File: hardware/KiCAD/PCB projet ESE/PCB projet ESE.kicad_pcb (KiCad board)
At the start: 4 copper layers, 57 x 54 mm, 104 parts, among them J1 Conn_01x06, J10 Conn_01x06, J11 Conn_01x06, J12 Conn_01x06, J13 Conn_01x06, J14 Conn_01x06, J15 Conn_01x06, J16 Conn_01x03, J17 Conn_01x03, J18 Conn_01x03, J19 Conn_01x03, J2 Conn_01x04, J20 Conn_01x03, J21 Conn_01x03, J22 Conn_01x03, J23 Conn_01x03, J24 Conn_01x03, J25 Conn_01x03, J26 USB_C_Receptacle_USB2.0_16P, J3 Conn_01x06, J4 Conn_01x06, J5 Conn_01x04, J6 Conn_01x02, J7 Conn_ST_STDC14, J8 Conn_01x06, J9 Conn_01x06, SW1 SW_SPST, SW2 472121010111, U1 ZXBM5210-SP, U2 ZXBM5210-SP, U3 STM32G474RETx, U4 ADXL343, U5 USBLC6-2SC6

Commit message: maj schematic et pinout
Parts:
- moved U3 0.59 mm to (249.0, 52.2)
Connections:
- net ADC renamed ADC1_IN2
- C13 pad 1: Net-(U3-VDDA) -> +3.3V
- C14 pad 2: Net-(U3-VDDA) -> +3.3V
- L1 pad 2: Net-(U3-VDDA) -> +3.3V
- U3 pad 29: Net-(U3-VDDA) -> +3.3V
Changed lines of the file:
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@@
 	(net 3 "+5V")
 	(net 4 "NRST")
-	(net 5 "ADC")
+	(net 5 "ADC1_IN2")
 	(net 6 "VBUS")
 	(net 7 "SDA TOF")
@@
 	(net 82 "unconnected-(SW2-Pad3)")
 	(net 83 "+7.4V")
-	(net 84 "Net-(U3-VDDA)")
-	(net 85 "Net-(C24-Pad1)")
-	(net 86 "Net-(C25-Pad1)")
-	(net 87 "PWM_Encodeur_B_Phase_1")
-	(net 88 "PWM_Encodeur_A_Phase_1")
-	(net 89 "unconnected-(J3-Pin_1-Pad1)")
-	(net 90 "unconnected-(J3-Pin_6-Pad6)")
-	(net 91 "PWM_Encodeur_B_Phase_2")
-	(net 92 "PWM_Encodeur_A_Phase_2")
-	(net 93 "Net-(J6-Pin_2)")
-	(net 94 "unconnected-(J26-SBU1-PadA8)")
-	(net 95 "Net-(J26-CC1)")
-	(net 96 "Net-(J26-CC2)")
-	(net 97 "unconnected-(J26-SBU2-PadB8)")
-	(net 98 "Net-(MP1-EN{slash}SYNC)")
-	(net 99 "PG_51")
-	(net 100 "Net-(MP2-EN{slash}SYNC)")
-	(net 101 "PG_52")
+	(net 84 "Net-(C24-Pad1)")
+	(net 85 "Net-(C25-Pad1)")
+	(net 86 "PWM_Encodeur_B_Phase_1")
+	(net 87 "PWM_Encodeur_A_Phase_1")
+	(net 88 "unconnected-(J3-Pin_1-Pad1)")
+	(net 89 "unconnected-(J3-Pin_6-Pad6)")
+	(net 90 "PWM_Encodeur_B_Phase_2")
+	(net 91 "PWM_Encodeur_A_Phase_2")
+	(net 92 "Net-(J6-Pin_2)")
+	(net 93 "unconnected-(J26-SBU1-PadA8)")
+	(net 94 "Net-(J26-CC1)")
+	(net 95 "Net-(J26-CC2)")
+	(net 96 "unconnected-(J26-SBU2-PadB8)")
+	(net 97 "Net-(MP1-EN{slash}SYNC)")
+	(net 98 "PG_51")
+	(net 99 "Net-(MP2-EN{slash}SYNC)")
+	(net 100 "PG_52")
 	(footprint "Connector_JST:JST_PH_B6B-PH-K_1x06_P2.00mm_Vertical"
 		(layer "F.Cu")
@@
 			(layers "F.Cu" "F.Mask" "F.Paste")
 			(roundrect_rratio 0.25)
-			(net 96 "Net-(J26-CC2)")
+			(net 95 "Net-(J26-CC2)")
 			(pintype "passive")
 		)
@@
 			(layers "*.Cu" "*.Mask")
 			(remove_unused_layers no)
-			(net 93 "Net-(J6-Pin_2)")
+			(net 92 "Net-(J6-Pin_2)")
 			(pinfunction "2")
 			(pintype "passive")
@@
 			(layers "F.Cu" "F.Mask" "F.Paste")
 			(roundrect_rratio 0.25)
-			(net 85 "Net-(C24-Pad1)")
+			(net 84 "Net-(C24-Pad1)")
 			(pintype "passive")
 		)
@@
 			(size 0.3 1.45)
 			(layers "F.Cu" "F.Mask" "F.Paste")
-			(net 95 "Net-(J26-CC1)")
+			(net 94 "Net-(J26-CC1)")
 			(pinfunction "CC1")
 			(pintype "bidirectional")
@@
 			(size 0.3 1.45)
 			(layers "F.Cu" "F.Mask" "F.Paste")
-			(net 94 "unconnected-(J26-SBU1-PadA8)")
+			(net 93 "unconnected-(J26-SBU1-PadA8)")
 			(pinfunction "SBU1")
 			(pintype "bidirectional+no_connect")
@@
 			(size 0.3 1.45)
 			(layers "F.Cu" "F.Mask" "F.Paste")
-			(net 96 "Net-(J26-CC2)")
+			(net 95 "Net-(J26-CC2)")
 			(pinfunction "CC2")
 			(pintype "bidirectional")
@@
 			(size 0.3 1.45)
 			(layers "F.Cu" "F.Mask" "F.Paste")
-			(net 97 "unconnected-(J26-SBU2-PadB8)")
+			(net 96 "unconnected-(J26-SBU2-PadB8)")
 			(pinfunction "SBU2")
 			(pintype "bidirectional+no_connect")
@@
 			(layers "*.Cu" "*.Mask")
 			(remove_unused_layers no)
-			(net 93 "Net-(J6-Pin_2)")
+			(net 92 "Net-(J6-Pin_2)")
 			(pinfunction "Pin_2")
 			(pintype "passive")
@@
 			(remove_unused_layers no)
 			(roundrect_rratio 0.208333)
-			(net 89 "unconnected-(J3-Pin_1-Pad1)")
+			(net 88 "unconnected-(J3-Pin_1-Pad1)")
 			(pinfunction "Pin_1")
 			(pintype "passive+no_connect")
@@
 			(layers "*.Cu" "*.Mask")
 			(remove_unused_layers no)
-			(net 90 "unconnected-(J3-Pin_6-Pad6)")
+			(net 89 "unconnected-(J3-Pin_6-Pad6)")
 			(pinfunction "Pin_6")
 			(pintype "passive+no_connect")
@@
 			(layers "F.Cu" "F.Mask" "F.Paste")
 			(roundrect_rratio 0.25)
-			(net 101 "PG_52")
+			(net 100 "PG_52")
 			(pintype "passive")
 		)
@@
 			(layers "*.Cu" "*.Mask")
 			(remove_unused_layers no)
-			(net 92 "PWM_Encodeur_A_Phase_2")
+			(net 91 "PWM_Encodeur_A_Phase_2")
 			(pinfunction "Pin_3")
 			(pintype "passive")
@@
 			(layers "*.Cu" "*.Mask")
 			(remove_unused_layers no)
-			(net 91 "PWM_Encodeur_B_Phase_2")
+			(net 90 "PWM_Encodeur_B_Phase_2")
 			(pinfunction "Pin_4")
 			(pintype "passive")
@@
 			(layers "F.Cu" "F.Mask" "F.Paste")
 			(roundrect_rratio 0.25)
-			(net 84 "Net-(U3-VDDA)")
+			(net 1 "+3.3V")
 			(pintype "passive")
 		)
@@
 			(layers "F.Cu" "F.Mask" "F.Paste")
 			(roundrect_rratio 0.15)
-			(net 101 "PG_52")
+			(net 100 "PG_52")
 			(pinfunction "PG")
 			(pintype "output")
@@
 			(layers "F.Cu" "F.Mask" "F.Paste")
 			(roundrect_rratio 0.15)
-			(net 100 "Net-(MP2-EN{slash}SYNC)")
+			(net 99 "Net-(MP2-EN{slash}SYNC)")
 			(pinfunction "EN/SYNC")
 			(pintype "input")
@@
 			(layers "F.Cu" "F.Mask" "F.Paste")
 			(roundrect_rratio 0.25)
-			(net 99 "PG_51")
+			(net 98 "PG_51")
 			(pintype "passive")
 		)
@@
 	(footprint "Package_QFP:LQFP-64_10x10mm_P0.5mm"
 		(layer "F.Cu")
-		(at 249.02 52.84)
+		(at 249 52.25)
 		(descr "LQFP, 64 Pin (https://www.analog.com/media/en/technical-documentation/data-sheets/ad7606_7606-6_7606-4.pdf), generated with kicad-footprint-generator ipc_gullwing_generator.py")
 		(tags "LQFP QFP")
@@
 			(layers "F.Cu" "F.Mask" "F.Paste")
 			(roundrect_rratio 0.25)
-			(net 99 "PG_51")
+			(net 98 "PG_51")
 			(pinfunction "PC13")
 			(pintype "bidirectional")
@@
 			(layers "F.Cu" "F.Mask" "F.Paste")
 			(roundrect_rratio 0.25)
-			(net 5 "ADC")
+			(net 5 "ADC1_IN2")
 			(pinfunction "PA1")
 			(pintype "bidirectional")
@@
 			(layers "F.Cu" "F.Mask" "F.Paste")
 			(roundrect_rratio 0.25)
-			(net 101 "PG_52")
+			(net 100 "PG_52")
 			(pinfunction "PC4")
 			(pintype "bidirectional")
@@
 			(layers "F.Cu" "F.Mask" "F.Paste")
 			(roundrect_rratio 0.25)
-			(net 88 "PWM_Encodeur_A_Phase_1")
+			(net 87 "PWM_Encodeur_A_Phase_1")
 			(pinfunction "PB0")
 			(pintype "bidirectional")
@@
 			(layers "F.Cu" "F.Mask" "F.Paste")
 			(roundrect_rratio 0.25)
-			(net 87 "PWM_Encodeur_B_Phase_1")
+			(net 86 "PWM_Encodeur_B_Phase_1")
 			(pinfunction "PB1")
 			(pintype "bidirectional")
@@
 			(layers "F.Cu" "F.Mask" "F.Paste")
 			(roundrect_rratio 0.25)
-			(net 84 "Net-(U3-VDDA)")
+			(net 1 "+3.3V")
 			(pinfunction "VDDA")
 			(pintype "power_in")
@@
 			(layers "F.Cu" "F.Mask" "F.Paste")
 			(roundrect_rratio 0.25)
-			(net 91 "PWM_Encodeur_B_Phase_2")
+			(net 90 "PWM_Encodeur_B_Phase_2")
 			(pinfunction "PB14")
 			(pintype "bidirectional")
@@
 			(layers "F.Cu" "F.Mask" "F.Paste")
 			(roundrect_rratio 0.25)
-			(net 92 "PWM_Encodeur_A_Phase_2")
+			(net 91 "PWM_Encodeur_A_Phase_2")
 			(pinfunction "PB6")
 			(pintype "bidirectional")
@@
 			(layers "F.Cu" "F.Mask" "F.Paste")
 			(roundrect_rratio 0.25)
-			(net 5 "ADC")
+			(net 5 "ADC1_IN2")
 			(pintype "passive")
 		)
@@
 			(layers "F.Cu" "F.Mask" "F.Paste")
 			(roundrect_rratio 0.25)
-			(net 5 "ADC")
+			(net 5 "ADC1_IN2")
 			(pintype "passive")
 		)
@@
 			(layers "F.Cu" "F.Mask" "F.Paste")
 			(roundrect_rratio 0.25)
-			(net 98 "Net-(MP1-EN{slash}SYNC)")
+			(net 97 "Net-(MP1-EN{slash}SYNC)")
 			(pintype "passive")
 		)
@@
 			(layers "F.Cu" "F.Mask" "F.Paste")
 			(roundrect_rratio 0.25)
-			(net 5 "ADC")
+			(net 5 "ADC1_IN2")
 			(pintype "passive")
 		)
@@
 			(layers "*.Cu" "*.Mask")
 			(remove_unused_layers no)
-			(net 88 "PWM_Encodeur_A_Phase_1")
+			(net 87 "PWM_Encodeur_A_Phase_1")
 			(pinfunction "Pin_3")
 			(pintype "passive")
@@
 			(layers "*.Cu" "*.Mask")
 			(remove_unused_layers no)
-			(net 87 "PWM_Encodeur_B_Phase_1")
+			(net 86 "PWM_Encodeur_B_Phase_1")
 			(pinfunction "Pin_4")
 			(pintype "passive")
@@
 			(layers "F.Cu" "F.Mask" "F.Paste")
 			(roundrect_rratio 0.25)
-			(net 100 "Net-(MP2-EN{slash}SYNC)")
+			(net 99 "Net-(MP2-EN{slash}SYNC)")
 			(pintype "passive")
 		)
@@
 			(layers "F.Cu" "F.Mask" "F.Paste")
 			(roundrect_rratio 0.25)
-			(net 86 "Net-(C25-Pad1)")
+			(net 85 "Net-(C25-Pad1)")
 			(pintype "passive")
 		)
@@
 			(layers "F.Cu" "F.Mask" "F.Paste")
 			(roundrect_rratio 0.25)
-			(net 84 "Net-(U3-VDDA)")
+			(net 1 "+3.3V")
 			(pintype "passive")
 		)
@@
 			(layers "F.Cu" "F.Mask" "F.Paste")
 			(roundrect_rratio 0.25)
-			(net 85 "Net-(C24-Pad1)")
+			(net 84 "Net-(C24-Pad1)")
 			(pintype "passive")
 		)
@@
 			(layers "F.Cu" "F.Mask" "F.Paste")
 			(roundrect_rratio 0.25)
-			(net 95 "Net-(J26-CC1)")
+			(net 94 "Net-(J26-CC1)")
 			(pintype "passive")
 		)
@@
 			(layers "F.Cu" "F.Mask" "F.Paste")
 			(roundrect_rratio 0.15)
-			(net 99 "PG_51")
+			(net 98 "PG_51")
 			(pinfunction "PG")
 			(pintype "output")
@@
 			(layers "F.Cu" "F.Mask" "F.Paste")
 			(roundrect_rratio 0.15)
-			(net 98 "Net-(MP1-EN{slash}SYNC)")
+			(net 97 "Net-(MP1-EN{slash}SYNC)")
 			(pinfunction "EN/SYNC")
 			(pintype "input")
@@
 			(layers "F.Cu" "F.Mask" "F.Paste")
 			(roundrect_rratio 0.25)
-			(net 84 "Net-(U3-VDDA)")
+			(net 1 "+3.3V")
 			(pintype "passive")
 		)
@@
 			(layers "F.Cu" "F.Mask" "F.Paste")
 			(roundrect_rratio 0.25)
-			(net 86 "Net-(C25-Pad1)")
+			(net 85 "Net-(C25-Pad1)")
 			(pintype "passive")
 		)

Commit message: update pcb
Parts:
- removed J17, J18, J19, J20, J21, J22, J23, J24, J25: Conn_01x03, Connector_JST:JST_PH_B3B-PH-K_1x03_P2.00mm_Vertical
- BUxxSD1, C1, C18, C19, C2, C20, C21, C22, C23, C24, C25, C26, C27, C28, C29, C3, C30, C31, C32, C33, C4, J1, J16, J4, J6, L2, L3, MP1, MP2, R10, R11, R12, R13, R14, R15, R16, R17, R18, R19, R20, R21, U1, U2: moved to B.Cu
- J10, J11, J12, J13, J14, J15, J3, J8, J9: footprint Connector_JST:JST_PH_B6B-PH-K_1x06_P2.00mm_Vertical -> Connector_JST:JST_SH_BM06B-SRSS-TB_1x06-1MP_P1.00mm_Vertical
- J2: footprint Connector_JST:JST_PH_B4B-PH-K_1x04_P2.00mm_Vertical -> Connector_JST:JST_SH_BM04B-SRSS-TB_1x04-1MP_P1.00mm_Vertical
- moved J7 180.2 mm to (84.3, 86.0)
- moved C4 175.5 mm to (87.8, 64.8), turned to -90 degrees
- moved U2 169.5 mm to (88.2, 70.0), turned to -90 degrees
- moved L1 167.8 mm to (95.2, 75.2), turned to 90 degrees
- moved C7 167.7 mm to (97.0, 75.2), turned to 90 degrees
- moved R3 167.1 mm to (96.3, 72.7), turned to -90 degrees
- moved R4 165.9 mm to (97.4, 72.7), turned to 90 degrees
- moved J4 165.1 mm to (83.0, 75.0), turned to 90 degrees
- moved J3 164.3 mm to (82.2, 59.5), turned to -90 degrees
- moved H2 164.1 mm to (84.0, 95.0)
- moved C14 157.6 mm to (108.0, 79.8)
- moved H1 155.3 mm to (84.0, 51.0)
- moved J5 154.0 mm to (93.0, 95.5)
- moved R2 150.1 mm to (113.5, 72.7), turned to 180 degrees
- moved R1 150.0 mm to (113.6, 71.6), turned to 180 degrees
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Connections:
- J1 pad 1: Encodeur phase A 1 -> Moteur - 1
- J1 pad 3: PWM_Encodeur_A_Phase_1 -> Encodeur_A_Phase_1
- J1 pad 4: PWM_Encodeur_B_Phase_1 -> Encodeur_B_Phase_1
- J1 pad 6: Encodeur Phase B 1 -> Moteur + 1
- J10 pad 1: INT -> INT_7
- J11 pad 1: INT -> INT_2
- J12 pad 1: INT -> INT_5
- J13 pad 1: INT -> INT_8
- J14 pad 1: INT -> INT_3
- J15 pad 1: INT -> INT_6
- J4 pad 1: Encodeur phase A 2 -> Moteur - 2
- J4 pad 3: PWM_Encodeur_A_Phase_2 -> Encodeur_A_Phase_2
- J4 pad 4: PWM_Encodeur_B_Phase_2 -> Encodeur_B_Phase_2
- J4 pad 6: Encodeur Phase B 2 -> Moteur + 2
- J8 pad 1: INT -> INT_1
- J9 pad 1: INT -> INT_4
- U1 pad 1: Encodeur phase A 1 -> Moteur + 1
- U1 pad 7: Encodeur Phase B 1 -> Moteur - 1
- U2 pad 1: Encodeur phase A 2 -> Moteur + 2
- U2 pad 7: Encodeur Phase B 2 -> Moteur - 2
- U3 pad 10: PWM_servo_3 -> unconnected-(U3-PC2-Pad10)
- U3 pad 11: PWM_servo_4 -> unconnected-(U3-PC3-Pad11)
- U3 pad 12: PWM_servo_5 -> INT_8
- U3 pad 21: STBY_IN -> XSHUT_8
- U3 pad 24: PWM_Encodeur_A_Phase_1 -> INT_4
- U3 pad 25: PWM_Encodeur_B_Phase_1 -> INT_3
- U3 pad 30: PWM_servo_7 -> INT_6
- U3 pad 33: PWM_servo_8 -> INT_5
- U3 pad 36: PWM_Encodeur_B_Phase_2 -> INT_7
- U3 pad 38: PWM FWD 2 -> Encodeur_A_Phase_2
- U3 pad 39: PWM REV 2 -> Encodeur_B_Phase_2
- U3 pad 56: PWM_servo_6 -> INT_2
- U3 pad 58: PWM_LED2 -> INT_1
- U3 pad 59: PWM_Encodeur_A_Phase_2 -> PWM FWD 2
- U3 pad 62: XSHUT_8 -> PWM REV 2
- U3 pad 8: PWM_servo_1 -> Encodeur_B_Phase_1
- U3 pad 9: PWM_servo_2 -> Encodeur_A_Phase_1
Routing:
- net +3.3V: track 0.00 -> 26.6 mm
- net +5V: track 0.00 -> 23.6 mm
- net +7.4V: track 0.00 -> 23.2 mm
- net VBUS: track 0.00 -> 12.8 mm
- net D+: track 0.00 -> 11.2 mm, vias 0 -> 2
- net GND: track 0.00 -> 10.6 mm
- net Net-(C25-Pad1): track 0.00 -> 5.98 mm
- net D-: track 0.00 -> 5.80 mm, vias 0 -> 2
- net Net-(MP1-BST): track 0.00 -> 5.24 mm, vias 0 -> 2
- net PG_52: track 0.00 -> 4.69 mm, vias 0 -> 2
- net Net-(MP1-VCC): track 0.00 -> 4.08 mm
- net Net-(MP1-EN/SYNC): track 0.00 -> 3.96 mm
- net Net-(MP2-VCC): track 0.00 -> 3.95 mm
- net ADC1_IN2: track 0.00 -> 3.84 mm
- net Net-(C26-Pad1): track 0.00 -> 3.73 mm
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
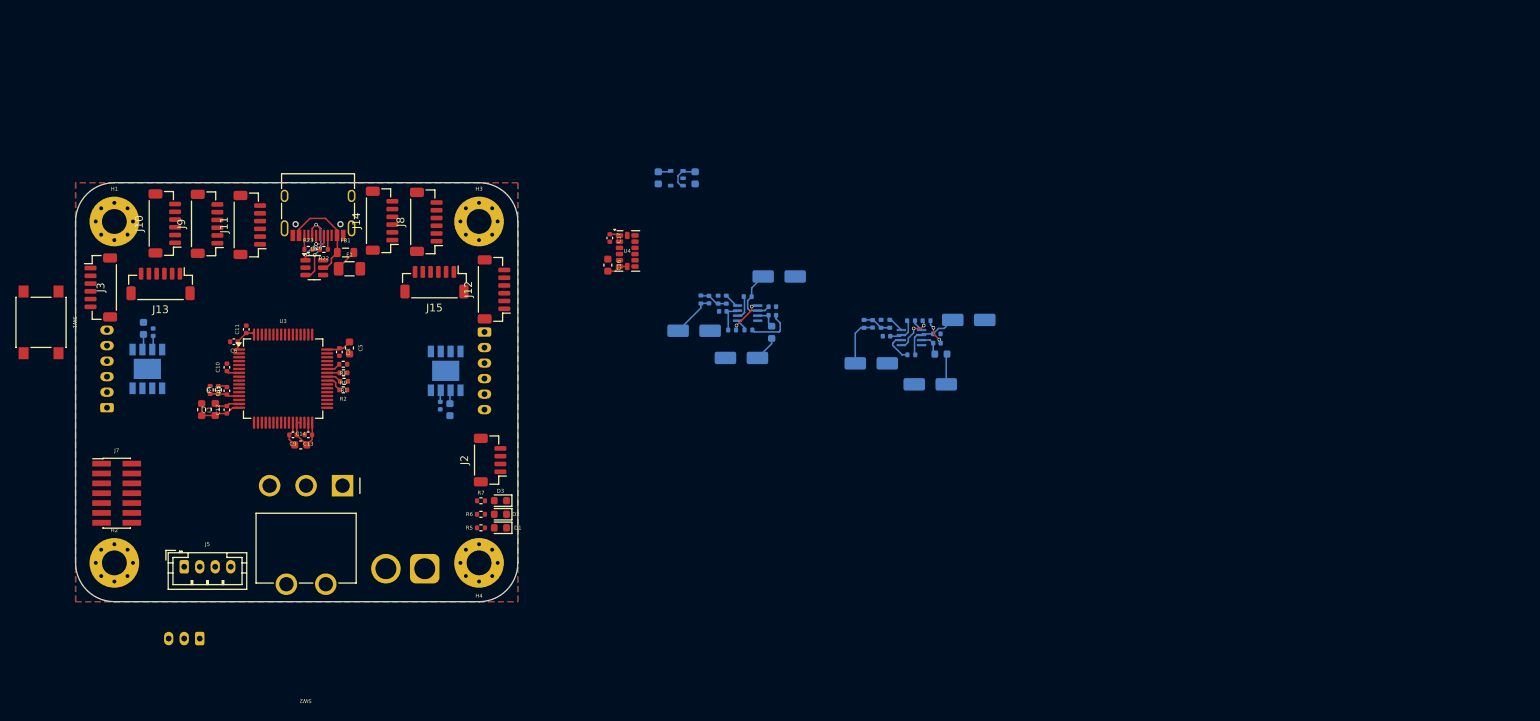
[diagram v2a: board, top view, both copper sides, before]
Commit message: modif pcb editor & sch for new uc pinout
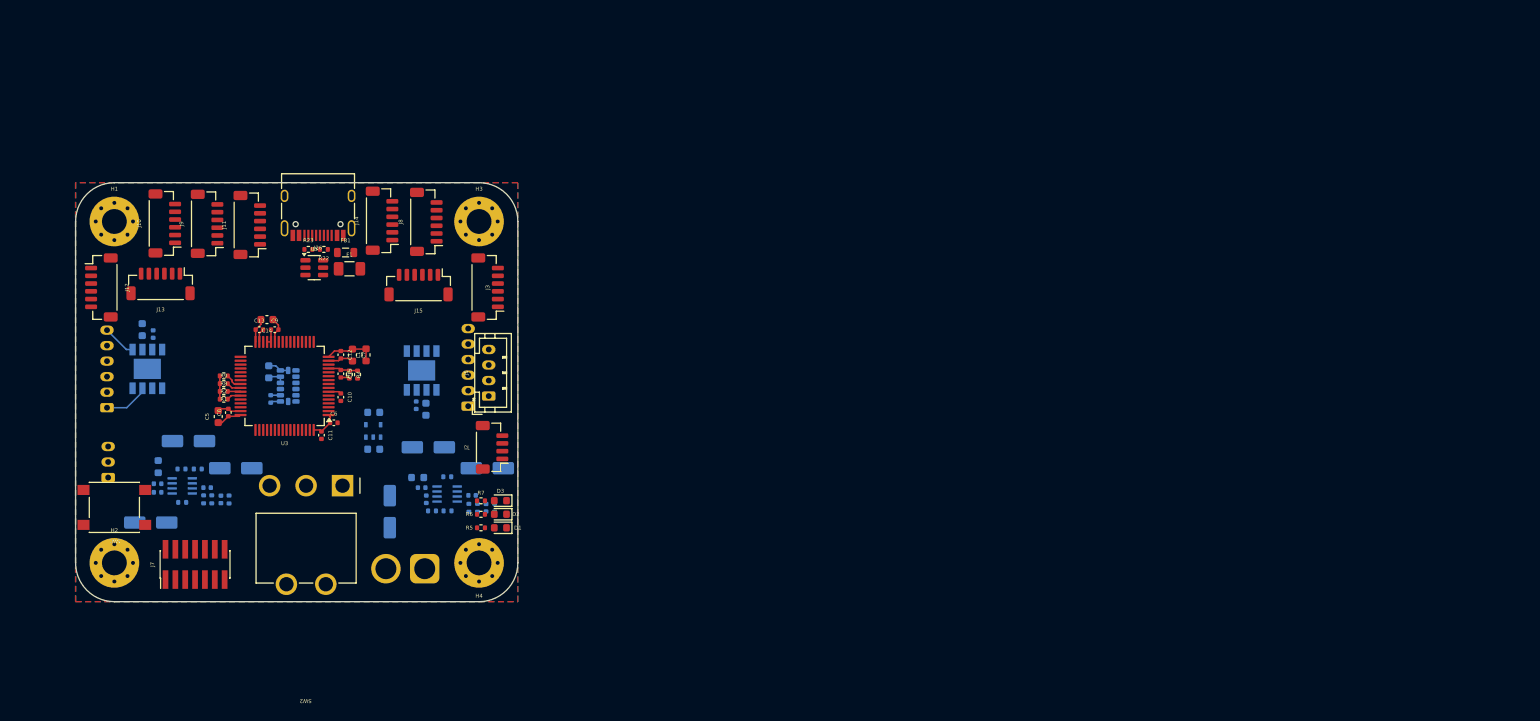
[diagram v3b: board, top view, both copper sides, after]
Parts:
- C16, C17, U4: moved to B.Cu
- moved C19 87.0 mm to (88.7, 89.8), turned to 0 degrees
- moved C23 82.8 mm to (89.6, 85.9), turned to 0 degrees
- moved C25 82.1 mm to (89.6, 84.8), turned to 0 degrees
- moved L3 80.9 mm to (89.7, 82.6), turned to 90 degrees
- moved C18 78.6 mm to (119.5, 88.4), turned to 90 degrees
- moved R11 77.6 mm to (92.7, 87.2), turned to 0 degrees
- moved MP2 76.2 mm to (92.8, 85.0), turned to 0 degrees
- moved R15 75.2 mm to (92.7, 82.9), turned to 180 degrees
- moved R17 72.1 mm to (95.5, 86.8), turned to -90 degrees
- moved C31 72.1 mm to (93.5, 79.3), turned to 180 degrees
- moved R13 71.2 mm to (94.8, 82.9), turned to 180 degrees
- moved C21 70.2 mm to (96.0, 85.3), turned to 0 degrees
- moved R19 70.2 mm to (96.5, 86.8), turned to -90 degrees
- moved L2 69.3 mm to (123.1, 84.0), turned to 180 degrees
- moved C22 69.2 mm to (124.2, 86.8), turned to 90 degrees
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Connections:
- J7 pad 11: GND -> unconnected-(J7-GNDDetect-Pad11)
- J7 pad 12: NRST -> unconnected-(J7-~{RST}-Pad12)
- J7 pad 13: UART_Debug_RX -> unconnected-(J7-VCP_RX-Pad13)
- J7 pad 14: UART_Debug_TX -> unconnected-(J7-VCP_TX-Pad14)
- J7 pad 4: SWDIO -> unconnected-(J7-JTMS/SWDIO-Pad4)
- J7 pad 6: SWCLK -> unconnected-(J7-JCLK/SWCLK-Pad6)
- U3 pad 11: unconnected-(U3-PC3-Pad11) -> INT 2
- U3 pad 12: INT_8 -> INT 1
- U3 pad 14: UART_Debug_TX -> UART_HC05_TX
- U3 pad 17: UART_Debug_RX -> UART_HC05_RX
- U3 pad 18: INT 1 -> INT_6
- U3 pad 19: INT 2 -> XSHUT_6
- U3 pad 20: Lidar Output  -> INT_1
- U3 pad 21: XSHUT_8 -> XSHUT_1
- U3 pad 22: PG_52 -> INT_3
- U3 pad 23: XSHUT_4 -> XSHUT_3
- U3 pad 24: INT_4 -> XSHUT_2
- U3 pad 25: INT_3 -> INT_2
- U3 pad 26: XSHUT_7 -> XSHUT_4
- U3 pad 3: unconnected-(U3-PC14-Pad3) -> Lidar Output 
- U3 pad 30: INT_6 -> INT_4
- U3 pad 33: INT_5 -> XSHUT_7
- U3 pad 34: XSHUT_5 -> INT_7
- U3 pad 35: XSHUT_6 -> INT_8
- U3 pad 36: INT_7 -> XSHUT_8
- U3 pad 37: XSHUT_3 -> INT_5
- U3 pad 38: Encodeur_A_Phase_2 -> Encodeur_B_Phase_2
- U3 pad 39: Encodeur_B_Phase_2 -> Encodeur_A_Phase_2
- U3 pad 40: Accel SCL -> SCL TOF
- U3 pad 41: Accel SDA -> SDA TOF
- U3 pad 42: SCL TOF -> Accel SCL
- U3 pad 43: SDA TOF -> Accel SDA
- U3 pad 44: XSHUT_1 -> XSHUT_5
- U3 pad 51: XSHUT_2 -> PG_52
- U3 pad 52: UART_HC05_TX -> UART_Debug_TX
- U3 pad 53: UART_HC05_RX -> UART_Debug_RX
- U3 pad 56: INT_2 -> unconnected-(U3-PB3-Pad56)
- U3 pad 58: INT_1 -> unconnected-(U3-PB5-Pad58)
- U3 pad 59: PWM FWD 2 -> PWM REV 2
- U3 pad 60: PWM REV 1 -> PWM FWD 2
- U3 pad 61: PWM FWD 1 -> PWM REV 1
- U3 pad 62: PWM REV 2 -> PWM FWD 1
- U3 pad 8: Encodeur_B_Phase_1 -> Encodeur_A_Phase_1
- U3 pad 9: Encodeur_A_Phase_1 -> Encodeur_B_Phase_1
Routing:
- net +5V: track 23.6 -> 0.00 mm
- net +7.4V: track 23.2 -> 0.00 mm
- net VBUS: track 12.8 -> 0.00 mm
- net D+: track 11.2 -> 0.00 mm, vias 2 -> 0
- net Net-(C25-Pad1): track 5.98 -> 0.00 mm
- net Moteur - 2: track 0.00 -> 5.89 mm
- net D-: track 5.80 -> 0.00 mm, vias 2 -> 0
- net GND: track 10.6 -> 16.3 mm
- net Net-(MP1-BST): track 5.24 -> 0.00 mm, vias 2 -> 0
- net PG_52: track 4.69 -> 0.00 mm, vias 2 -> 0
- net Moteur + 2: track 0.00 -> 4.33 mm
- net Net-(MP1-VCC): track 4.08 -> 0.00 mm
- net Net-(MP1-EN/SYNC): track 3.96 -> 0.00 mm
- net Net-(MP2-VCC): track 3.95 -> 0.00 mm
- net Net-(C26-Pad1): track 3.73 -> 0.00 mm
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- added copper zone on In2.Cu, net Net-(J6-Pin_2)

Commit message: maj
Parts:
- turned F1 to 180 degrees
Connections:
- J7 pad 11: unconnected-(J7-GNDDetect-Pad11) -> GND
- J7 pad 12: unconnected-(J7-~{RST}-Pad12) -> NRST
- J7 pad 13: unconnected-(J7-VCP_RX-Pad13) -> UART_Debug_RX
- J7 pad 14: unconnected-(J7-VCP_TX-Pad14) -> UART_Debug_TX
- J7 pad 4: unconnected-(J7-JTMS/SWDIO-Pad4) -> SWDIO
- J7 pad 6: unconnected-(J7-JCLK/SWCLK-Pad6) -> SWCLK
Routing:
- net SDA TOF: track 1.88 -> 37.6 mm, vias 0 -> 2
- net SCL TOF: track 2.20 -> 32.3 mm
- net NRST: track 1.67 -> 24.6 mm
- net Encodeur_B_Phase_1: track 0.00 -> 19.3 mm
- net Encodeur_A_Phase_1: track 0.00 -> 18.7 mm, vias 0 -> 1
- net Moteur - 1: track 0.00 -> 13.3 mm, vias 0 -> 1
- net Moteur + 1: track 0.00 -> 9.59 mm
- net D+: track 0.00 -> 9.33 mm, vias 0 -> 2
- net Accel SDA: track 1.84 -> 10.4 mm, vias 0 -> 1
- net Accel SCL: track 1.67 -> 9.21 mm, vias 0 -> 1
- net PG_52: track 0.00 -> 4.80 mm, vias 0 -> 2
- net Net-(MP1-BST): track 0.00 -> 4.75 mm, vias 0 -> 2
- net INT 1: track 0.00 -> 4.31 mm, vias 0 -> 1
- net INT 2: track 0.00 -> 4.24 mm, vias 0 -> 1
- net Net-(MP1-VCC): track 0.00 -> 4.08 mm
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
